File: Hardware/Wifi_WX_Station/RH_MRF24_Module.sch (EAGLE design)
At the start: 7 parts, among them M1 MRF24WB0MA

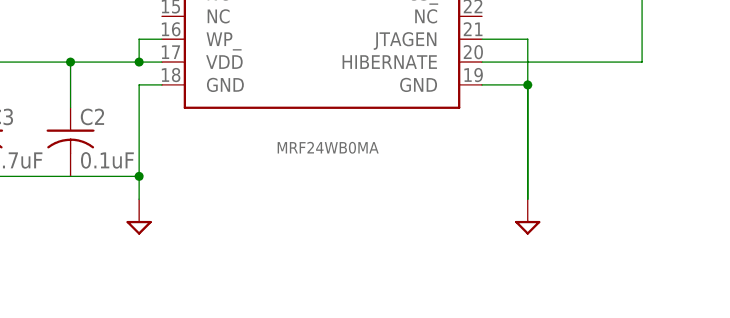
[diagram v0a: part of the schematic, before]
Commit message: Modified the RF carrier slightly with longer pads for easier soldering.
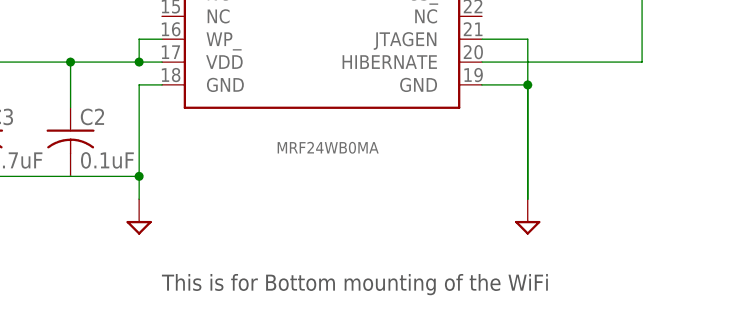
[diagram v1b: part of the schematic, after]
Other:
- note added: "This is for Bottom mounting of the WiFi"
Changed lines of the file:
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@@
 <?xml version="1.0" encoding="utf-8"?>
 <!DOCTYPE eagle SYSTEM "eagle.dtd">
-<eagle version="6.3">
+<eagle version="6.5.0">
 <drawing>
 <settings>
@@
 <sheet>
 <plain>
+<text x="12.7" y="-12.7" size="1.778" layer="97">This is for Bottom mounting of the WiFi</text>
 </plain>
 <instances>
